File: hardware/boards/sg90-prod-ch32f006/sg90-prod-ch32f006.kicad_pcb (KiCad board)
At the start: 4 copper layers, 12.5 x 10 mm, 21 parts, among them J1 Servo Input, J2 Debug, J3 Motor, J4 Potentiometer, Q1 BRCS150P02ZJ, U1 CH32V006F8U6, U2 DRV8837C, U3 74LVC1G07

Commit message: re-organize shared folders
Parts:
- removed C7: 10µF, Capacitor_SMD:C_0603_1608Metric
- removed R9: 1kΩ, Resistor_SMD:R_0402_1005Metric
- added D1: PESD5V0L1UL, Diode_SMD:D_SOD-882, F.Cu at (109.6, 84.4)
- added NT1: NetTie_2, shared:NetTie-2_SMD_0.2mm, F.Cu at (121.3, 75.5)
- added NT2: NetTie_2, shared:NetTie-2_SMD_0.2mm, F.Cu at (121.3, 77.0)
- added NT3: NetTie_2, shared:NetTie-2_SMD_0.2mm, F.Cu at (121.3, 78.5)
- added NT4: NetTie_2, shared:NetTie-2_SMD_0.2mm, F.Cu at (121.3, 80.0)
- added R7: 10kΩ, Resistor_SMD:R_0402_1005Metric, F.Cu at (0.95, 0.49)
- C1: value 0.1µF -> 10µF; footprint Capacitor_SMD:C_0402_1005Metric -> Capacitor_SMD:C_0603_1608Metric
- C2: value 47nF -> 0.1µF
- C6: value 10µF -> 47nF; footprint Capacitor_SMD:C_0603_1608Metric -> Capacitor_SMD:C_0402_1005Metric
- J1: footprint common:Servo_Output_Pads -> shared:Servo_Output_Pads; moved to B.Cu
- J2: footprint common:Debug_Pads_1x4_P1.27mm -> shared:Debug_Pads_1x4_P1.27mm
- J3: footprint common:Motor_Wire_Pads -> shared:Motor_Wire_Pads; moved to B.Cu
- J4: footprint common:Pot_Wire_Pads -> shared:Pot_Wire_Pads; moved to B.Cu
- Q1: footprint common:DFN-6L_L2.0-W2.0-P0.65-BL_BRCS300PXX -> shared:DFN-6L_L2.0-W2.0-P0.65-BL_BRCS300PXX
- R2: value 0.1Ω 1% -> 1kΩ; footprint Resistor_SMD:R_0603_1608Metric -> Resistor_SMD:R_0402_1005Metric
- R4: value 10kΩ -> 0.1Ω 1%; footprint Resistor_SMD:R_0402_1005Metric -> Resistor_SMD:R_0603_1608Metric
- U1: value CH32V006F8U6 -> 74LVC1G07; footprint common:UQFN-20_L3.0-W3.0-P0.40-BL-EP1.7 -> shared:TDFN-6_L1.0-W1.0-P0.35-BL
- U3: value 74LVC1G07 -> CH32V006F8U6; footprint common:TDFN-6_L1.0-W1.0-P0.35-BL -> shared:UQFN-20_L3.0-W3.0-P0.40-BL-EP1.7
- moved R2 25.9 mm to (125.5, 83.6)
- moved C2 20.3 mm to (125.4, 104.0), turned to -90 degrees
- moved C5 18.4 mm to (119.2, 104.8)
- moved R5 18.1 mm to (125.2, 101.5)
- moved R3 16.6 mm to (119.7, 99.9)
- moved C6 15.8 mm to (122.0, 87.6)
- moved C1 15.1 mm to (107.5, 84.5), turned to -90 degrees
- moved U1 14.4 mm to (121.8, 103.2)
- moved U3 14.2 mm to (117.8, 83.2)
- moved R1 13.9 mm to (118.7, 102.8)
- moved Q1 9.31 mm to (117.9, 90.5)
- moved J2 7.46 mm to (107.9, 106.0)
- moved R4 4.71 mm to (102.0, 96.8)
- moved C3 4.57 mm to (101.0, 93.0), turned to 180 degrees
- moved C4 2.17 mm to (102.9, 93.0), turned to 0 degrees
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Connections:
- C2 pad 1: /SEN_POT -> +5V
- C6 pad 1: +5V -> /SEN_POT
- J3 pad 1: /MOT_B -> /MOT_A
- J3 pad 2: /MOT_A -> /MOT_B
- J4 pad 3: /V_MCU -> +5V
- R1 pad 1: /nRST -> Net-(Q1-G)
- R2 pad 1: /GND_MOT -> +5V
- R2 pad 2: GND -> /DATA
- R4 pad 1: Net-(Q1-G) -> GND
- R4 pad 2: GND -> /GND_MOT
- U1 pad 1: /nRST -> unconnected-(U1-NC-Pad1)
- U1 pad 2: /GND_MOT -> /UART_TX
- U1 pad 3: /GND_MOT -> GND
- U1 pad 4: GND -> /DATA
- U3 pad 1: unconnected-(U3-NC-Pad1) -> /nRST
- U3 pad 2: /UART_TX -> /SEN_I
- U3 pad 3: GND -> /SEN_I
- U3 pad 4: /DATA -> GND

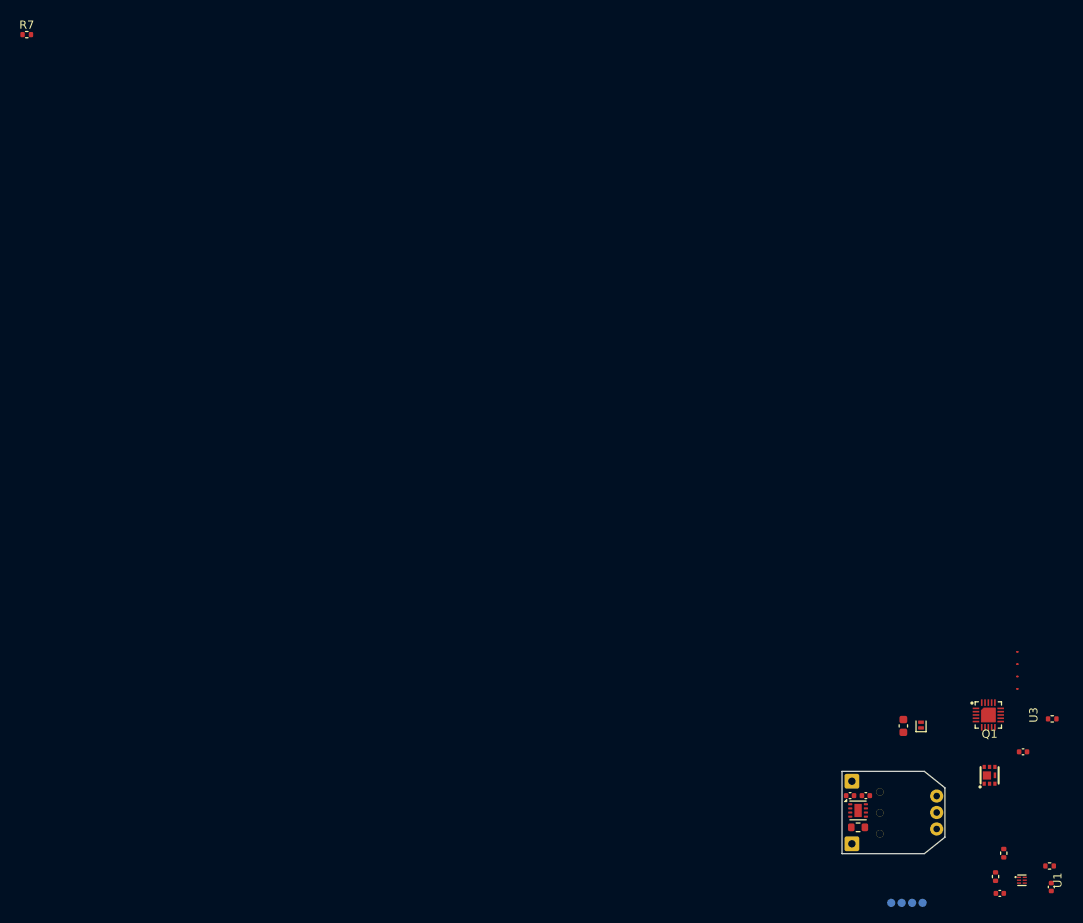
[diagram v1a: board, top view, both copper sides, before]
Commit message: completed initial pass n sg90-prod-ch32f006
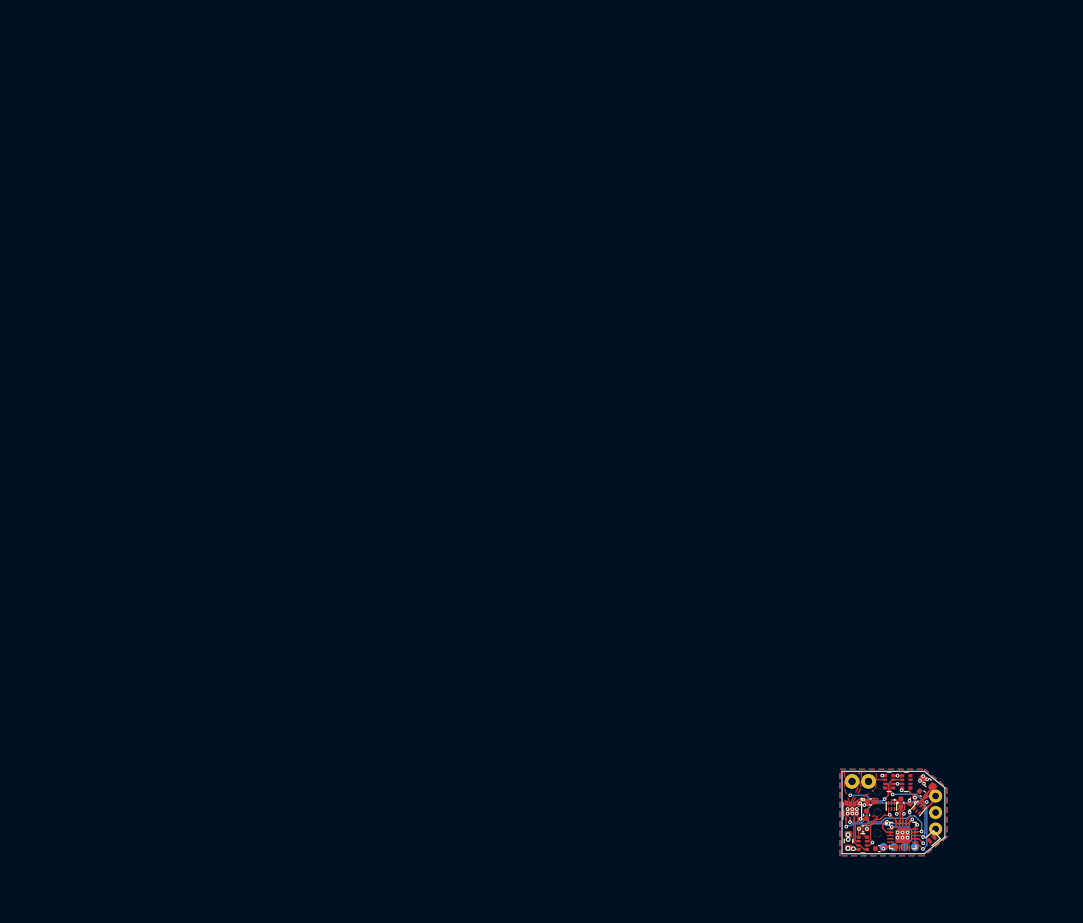
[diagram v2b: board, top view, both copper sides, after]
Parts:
- removed NT3, NT4: NetTie_2, shared:NetTie-2_SMD_0.2mm
- removed Q1: BRCS150P02ZJ, shared:DFN-6L_L2.0-W2.0-P0.65-BL_BRCS300PXX
- removed R2, R5: 1kΩ, Resistor_SMD:R_0402_1005Metric
- removed R3, R7: 10kΩ, Resistor_SMD:R_0402_1005Metric
- removed R4: 0.1Ω 1%, Resistor_SMD:R_0603_1608Metric
- added C2: 1uF, Capacitor_SMD:C_0402_1005Metric, F.Cu at (109.8, 92.7)
- added C3: 1uF, Capacitor_SMD:C_0402_1005Metric, F.Cu at (108.6, 93.6)
- added RN1: 20kΩ, Resistor_SMD:R_Array_Convex_4x0402, F.Cu at (105.7, 91.3)
- added RN2: 10kΩ, Resistor_SMD:R_Array_Convex_4x0402, F.Cu at (107.8, 91.3)
- added RN3: 1kΩ, Resistor_SMD:R_Array_Convex_4x0402, F.Cu at (102.5, 98.7)
- added U1: LDK220PU33R, shared:DFN-6_L1.3-W1.2-P0.40-BL, F.Cu at (109.3, 94.5)
- J2: renamed from J3; moved to F.Cu
- R1: value 10kΩ -> 0.1Ω 1%; footprint Resistor_SMD:R_0402_1005Metric -> Resistor_SMD:R_0603_1608Metric
- U3: renamed from U2; value DRV8837C -> DRV8837DSGR-JSM
- moved NT2 25.6 mm to (105.0, 96.7), turned to 90 degrees
- moved NT1 25.2 mm to (106.4, 95.8), turned to 135 degrees
- moved C5 21.6 mm to (102.5, 97.0), turned to 0 degrees
- moved C4 20.9 mm to (107.2, 93.8), turned to 90 degrees
- moved R1 18.4 mm to (100.8, 98.5)
- moved U2 18.2 mm to (106.0, 94.2), turned to 180 degrees
- moved U4 18.0 mm to (107.4, 97.8)
- moved C8 15.6 mm to (104.5, 99.4), turned to 180 degrees
- moved D1 13.9 mm to (110.9, 98.2), turned to -140.5 degrees
- moved C1 7.51 mm to (110.4, 91.4), turned to 140.5 degrees
- moved J3 6.84 mm to (107.0, 99.2), turned to 0 degrees
- moved J2 3.92 mm to (102.2, 91.2), turned to 180 degrees
- moved C6 3.09 mm to (103.0, 95.3), turned to 90 degrees
- moved C7 0.94 mm to (103.5, 93.7)
- moved U3 0.72 mm to (101.2, 94.9), turned to -90 degrees
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- renumbered C2 to C4, C6 to C5, C3 to C6, C4 to C7, C5 to C8, J2 to J3, U1 to U2, U3 to U4
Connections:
- net /MOT_PH renamed /MOT_IN2
- net /MOT_PWM renamed /MOT_IN1
- C1 pad 1: +5V -> /V_BAT
- C4 pad 1: +5V -> +3.3V
- C6 pad 1: +5V -> +3.3V
- C7 pad 1: +5V -> /V_BAT
- C8 pad 1: +5V -> +3.3V
- J1 pad 1: GND -> /V_BAT
- J1 pad 2: /V_IN -> GND
- J3 pad 1: GND -> +3.3V
- J3 pad 2: /V_IN -> GND
- J4 pad 1: GND -> +3.3V
- J4 pad 3: +5V -> GND
- NT1 pad 1: /DATA -> /UART_RX
- NT1 pad 2: /UART_RX -> /DATA
- R1 pad 1: Net-(Q1-G) -> GND
- R1 pad 2: GND -> /GND_MOT
- U2 pad 6: +5V -> +3.3V
- U3 pad 1: +5V -> /V_BAT
- U3 pad 7: /MOT_EN -> /nSLEEP
- U3 pad 8: +5V -> +3.3V
- U4 pad 11: /SEN_POT -> /SEN_A
- U4 pad 16: /SEN_A -> /SEN_POT
- U4 pad 18: unconnected-(U3-PD4/T1/T2/SCK_/OPO0/A7-Pad18) -> /SEN_BAT
- U4 pad 19: unconnected-(U3-PD5/T2/TX/RX_/MISO_/A5-Pad19) -> /UART_TX
- U4 pad 20: unconnected-(U3-PD6/T2/RX/TX_/MOSI_/A6-Pad20) -> /UART_RX
- U4 pad 6: +5V -> +3.3V
- U4 pad 7: /UART_TX -> unconnected-(U4-PC0/T1C1N_/T1/T2/TX_/MOSI_-Pad7)
- U4 pad 8: /UART_RX -> unconnected-(U4-PC1/T1C2N_/T2/RX_/SDA/NSS-Pad8)
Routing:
- net /MOT_IN1: track 0.00 -> 16.4 mm, vias 0 -> 2
- net /SEN_A: track 0.00 -> 15.4 mm, vias 0 -> 2
- net /DATA: track 0.00 -> 13.9 mm, vias 0 -> 1
- net /MOT_IN2: track 0.00 -> 12.8 mm, vias 0 -> 2
- net +3.3V: track 0.00 -> 11.9 mm, vias 0 -> 4
- net /nRST: track 0.00 -> 11.2 mm, vias 0 -> 2
- net /SEN_POT: track 0.00 -> 9.21 mm, vias 0 -> 2
- net /SEN_BAT: track 0.00 -> 8.62 mm, vias 0 -> 2
- net /MOT_EN: track 0.00 -> 8.54 mm, vias 0 -> 2
- net /MOT_B: track 0.00 -> 7.72 mm, vias 0 -> 2
- net /SEN_B: track 0.00 -> 7.18 mm, vias 0 -> 2
- net /V_BAT: track 0.00 -> 6.26 mm, vias 0 -> 4
- net /UART_TX: track 0.00 -> 5.02 mm
- net /nSLEEP: track 0.00 -> 4.80 mm
- net /POT: track 0.00 -> 4.47 mm
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- added copper zone on In2.Cu, net +3.3V
- added copper zone on F.Cu, net /GND_MOT
- added copper zone on In3.Cu, net /GND_MOT
- added copper zone on In4.Cu, net /GND_MOT
- added copper zone on F.Cu, net /MOT_A
- added copper zone on F.Cu, net /MOT_B
- added copper zone on F.Cu, net /V_BAT
- added copper zone on In5.Cu, net /V_BAT
- added copper zone on B.Cu, net GND
- added copper zone on F.Cu, net GND
- added copper zone on In1.Cu, net GND
- added copper zone on In6.Cu, net GND
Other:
- copper layers 4 -> 8

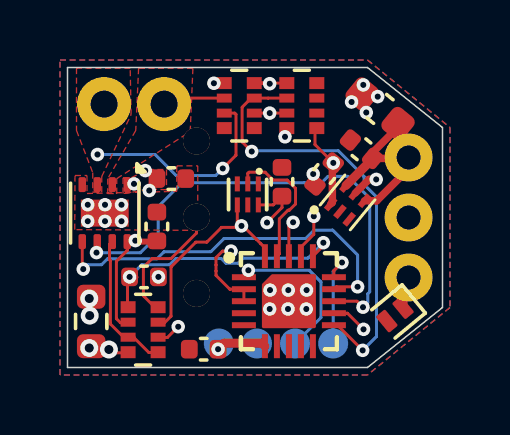
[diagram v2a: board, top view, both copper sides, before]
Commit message: finished first pass design of sg90-prod-ch32f006. It is ready for production
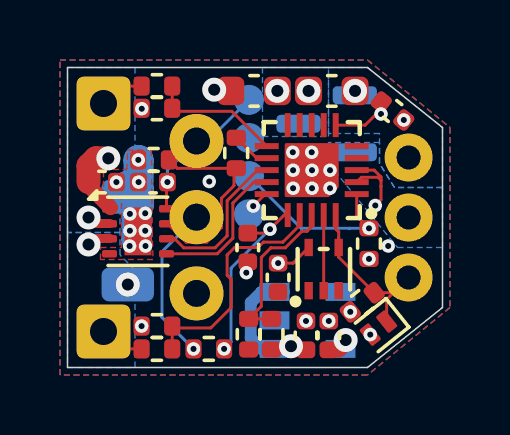
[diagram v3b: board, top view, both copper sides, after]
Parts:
- removed RN1: 20kΩ, Resistor_SMD:R_Array_Convex_4x0402
- removed RN2: 10kΩ, Resistor_SMD:R_Array_Convex_4x0402
- removed RN3: 1kΩ, Resistor_SMD:R_Array_Convex_4x0402
- added C9: 10µF, Capacitor_SMD:C_0603_1608Metric, F.Cu at (106.2, 90.8)
- added Q1: AO3401A, Package_TO_SOT_SMD:SOT-23, B.Cu at (108.6, 91.9)
- added R10: 10kΩ, Resistor_SMD:R_0402_1005Metric, F.Cu at (103.0, 91.4)
- added R11: 20kΩ, Resistor_SMD:R_0402_1005Metric, F.Cu at (103.0, 99.4)
- added R12: 10kΩ, Resistor_SMD:R_0402_1005Metric, F.Cu at (103.0, 98.6)
- added R2: 4.7kΩ, Resistor_SMD:R_0402_1005Metric, F.Cu at (104.7, 99.4)
- added R3: 10kΩ, Resistor_SMD:R_0402_1005Metric, F.Cu at (102.9, 93.1)
- added R4: 0.1Ω 1%, Resistor_SMD:R_1206_3216Metric, B.Cu at (102.0, 95.8)
- added R5: 330Ω, Resistor_SMD:R_0402_1005Metric, F.Cu at (105.6, 92.8)
- added R6: 10kΩ, Resistor_SMD:R_0402_1005Metric, F.Cu at (110.0, 95.9)
- added R7: 20kΩ, Resistor_SMD:R_0402_1005Metric, F.Cu at (106.8, 98.9)
- added R8: 10kΩ, Resistor_SMD:R_0402_1005Metric, F.Cu at (106.0, 98.9)
- added R9: 20kΩ, Resistor_SMD:R_0402_1005Metric, F.Cu at (103.0, 90.6)
- C2, C3: value 1uF -> 1µF
- C5: value 47nF -> 0.1µF
- R1: value 0.1Ω 1% -> 1kΩ; footprint Resistor_SMD:R_0603_1608Metric -> Resistor_SMD:R_0402_1005Metric
- U1: value LDK220PU33R -> TPAP2210K-3.3TRG1; footprint shared:DFN-6_L1.3-W1.2-P0.40-BL -> shared:SOT-23-5_L2.9-W1.6-P0.95-LS2.8-BR; moved to B.Cu
- U2: value 74LVC1G07 -> SN74LVC1G07DRLR_C19829624; footprint shared:TDFN-6_L1.0-W1.0-P0.35-BL -> shared:SOT-553-5_L1.6-W1.2-P0.50-LS1.6-BL
- moved C8 10.1 mm to (110.8, 91.4), turned to -38.659 degrees
- moved R1 9.06 mm to (109.8, 97.8), turned to 38.659 degrees
- moved C2 6.48 mm to (108.0, 98.9), turned to 90 degrees
- moved J3 6.28 mm to (106.0, 93.0), turned to -90 degrees
- moved NT2 6.18 mm to (110.5, 93.9), turned to -90 degrees
- moved C3 5.38 mm to (108.7, 98.9), turned to 90 degrees
- moved U4 4.44 mm to (108.1, 93.4), turned to 90 degrees
- moved U1 4.15 mm to (108.0, 98.4), turned to 180 degrees
- moved J2 3.92 mm to (101.2, 95.0), turned to -90 degrees
- moved C5 3.60 mm to (106.0, 96.0), turned to -90 degrees
- moved U2 3.55 mm to (108.5, 96.7), turned to 0 degrees
- moved C4 3.19 mm to (107.0, 97.0), turned to -90 degrees
- moved NT1 2.68 mm to (109.0, 95.6), turned to -90 degrees
- moved C7 2.31 mm to (101.2, 93.8)
- moved C1 1.72 mm to (108.8, 90.8), turned to 0 degrees
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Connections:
- net /MOT_A renamed /OUTA
- net /MOT_B renamed /OUTB
- net /MOT_IN1 renamed /IN1
- net /MOT_IN2 renamed /IN2
- net /SEN_I renamed /ISNS
- net /SEN_POT renamed /VPOS
- net /UART_RX renamed /RX
- net /UART_TX renamed /TX
- C1 pad 1: /V_BAT -> /VSYS
- C2 pad 1: /V_BAT -> /VSYS
- C6 pad 2: /GND_MOT -> PGND
- C7 pad 1: /V_BAT -> /VSYS
- C7 pad 2: /GND_MOT -> PGND
- J1 pad 1: /V_BAT -> GND
- J1 pad 2: GND -> VIN
- NT2 pad 2: /GND_MOT -> PGND
- R1 pad 1: GND -> +3.3V
- R1 pad 2: /GND_MOT -> /DATA
- U1 pad 1: +3.3V -> /VSYS
- U1 pad 2: unconnected-(U1-N/C-Pad2) -> GND
- U1 pad 3: unconnected-(U1-ADJ/NC-Pad3) -> /VSYS
- U1 pad 4: /V_BAT -> unconnected-(U1-NC-Pad4)
- U1 pad 5: GND -> +3.3V
- U2 pad 5: unconnected-(U2-NC-Pad5) -> +3.3V
- U3 pad 1: /V_BAT -> /VSYS
- U3 pad 4: /GND_MOT -> PGND
- U3 pad 9: /GND_MOT -> PGND
- U4 pad 11: /SEN_A -> /VSNA
- U4 pad 12: /MOT_EN -> /EN
- U4 pad 17: /SEN_B -> /VSNB
- U4 pad 18: /SEN_BAT -> /VINS
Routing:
- net /SEN_A: track 15.4 -> 0.00 mm, vias 2 -> 0
- net /IN1: track 16.4 -> 5.22 mm, vias 2 -> 0
- net /SEN_BAT: track 8.62 -> 0.00 mm, vias 2 -> 0
- net /MOT_EN: track 8.54 -> 0.00 mm, vias 2 -> 0
- net /DATA: track 13.9 -> 5.44 mm, vias 1 -> 0
- net /VSYS: track 0.00 -> 8.30 mm, vias 0 -> 4
- net /VSNB: track 0.00 -> 8.01 mm
- net /IN2: track 12.8 -> 5.02 mm, vias 2 -> 0
- net /SEN_B: track 7.18 -> 0.00 mm, vias 2 -> 0
- net /V_BAT: track 6.26 -> 0.00 mm, vias 4 -> 0
- net /VINS: track 0.00 -> 5.47 mm
- net /OUTB: track 7.72 -> 2.32 mm, vias 2 -> 1
- net /nRST: track 11.2 -> 6.03 mm, vias 2 -> 1
- net /VSNA: track 0.00 -> 4.42 mm
- net PGND: track 0.00 -> 3.48 mm, vias 0 -> 10
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- added copper zone on B.Cu, net /OUTA
- added copper zone on B.Cu, net /OUTB
- added copper zone on B.Cu, net /VSYS
- added copper zone on In4.Cu, net /VSYS
- added copper zone on F.Cu, net PGND
- added copper zone on In3.Cu, net PGND
- added copper zone on B.Cu, net VIN
- removed copper zone on F.Cu, net /GND_MOT
- removed copper zone on In3.Cu, net /GND_MOT
- removed copper zone on In4.Cu, net /GND_MOT
- removed copper zone on F.Cu, net /OUTA
- removed copper zone on F.Cu, net /OUTB
- removed copper zone on F.Cu, net /V_BAT
- removed copper zone on In5.Cu, net /V_BAT
- removed copper zone on In6.Cu, net GND
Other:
- copper layers 8 -> 6
- board text added: "+"
- board text added: "-"
- board text added: "R"
- board text added: "S"

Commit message: redid the PCB after finding a bunch of issues
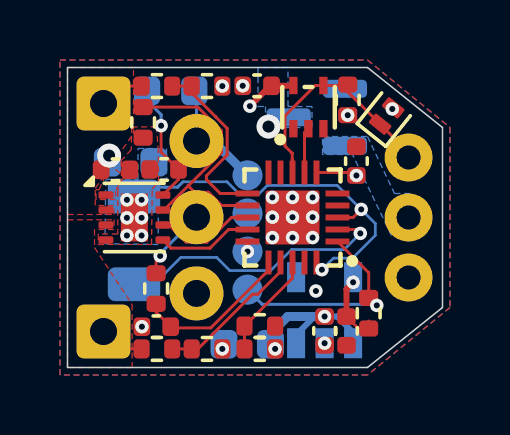
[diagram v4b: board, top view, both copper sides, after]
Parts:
- removed R5: 330Ω, Resistor_SMD:R_0402_1005Metric
- added FB1: 600Ω@100MHz, Inductor_SMD:L_0603_1608Metric, B.Cu at (103.4, 90.8)
- added NT3: NetTie_2, shared:NetTie-2_SMD_0.2mm, B.Cu at (103.2, 96.9)
- C1, NT2: moved to B.Cu
- C8: value 0.1µF -> 10µF; footprint Capacitor_SMD:C_0402_1005Metric -> Capacitor_SMD:C_0603_1608Metric; moved to B.Cu
- C9: value 10µF -> 0.1µF; footprint Capacitor_SMD:C_0603_1608Metric -> Capacitor_SMD:C_0402_1005Metric
- moved C1 8.90 mm to (106.0, 99.2), turned to 180 degrees
- moved C8 8.90 mm to (102.1, 93.2), turned to 0 degrees
- moved NT2 7.28 mm to (103.2, 94.0), turned to 180 degrees
- moved D1 7.07 mm to (110.6, 91.6), turned to 51.341 degrees
- moved R1 6.76 mm to (109.3, 91.1), turned to 90 degrees
- moved C4 6.43 mm to (106.3, 90.6), turned to 180 degrees
- moved U2 5.42 mm to (108.0, 91.3)
- moved C9 4.14 mm to (109.6, 93.1), turned to 90 degrees
- moved C5 4.03 mm to (103.0, 98.6), turned to 180 degrees
- moved NT1 3.04 mm to (107.5, 93.0), turned to 90 degrees
- moved R2 2.67 mm to (103.0, 97.4), turned to -90 degrees
- moved J3 2.52 mm to (106.0, 95.5)
- moved R6 2.32 mm to (110.0, 98.2)
- moved R12 1.83 mm to (104.7, 99.4), turned to 0 degrees
- moved R10 1.83 mm to (104.7, 90.6), turned to 0 degrees
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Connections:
- C6 pad 1: +3.3V -> /3V3_DRV
- C8 pad 1: +3.3V -> /VSYS
- C8 pad 2: GND -> PGND
- C9 pad 1: /VSYS -> +3.3V
- J3 pad 3: /nRST -> /SWDIO
- J3 pad 4: /SWDIO -> /nRST
- NT2 pad 1: /ISNS -> /ISNS+
- R3 pad 1: /nSLEEP -> /EN
- R4 pad 1: PGND -> GND
- R4 pad 2: GND -> PGND
- U3 pad 7: /nSLEEP -> /EN
- U3 pad 8: +3.3V -> /3V3_DRV
- U4 pad 19: /TX -> unconnected-(U4-PD5/T2/TX/RX_/MISO_/A5-Pad19)
- U4 pad 2: /ISNS -> /ISNS-
- U4 pad 20: /RX -> /ISNS+
- U4 pad 3: /ISNS -> /ISNS+
- U4 pad 7: unconnected-(U4-PC0/T1C1N_/T1/T2/TX_/MOSI_-Pad7) -> /TX
- U4 pad 8: unconnected-(U4-PC1/T1C2N_/T2/RX_/SDA/NSS-Pad8) -> /RX
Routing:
- net /ISNS+: track 0.00 -> 11.4 mm, vias 0 -> 2
- net /ISNS-: track 0.00 -> 8.30 mm, vias 0 -> 1
- net /EN: track 1.30 -> 8.66 mm
- net /nSLEEP: track 6.91 -> 0.00 mm
- net /3V3_DRV: track 0.00 -> 4.13 mm, vias 0 -> 1
- net PGND: track 3.48 -> 0.00 mm, vias 10 -> 6
- net /VSNB: track 8.01 -> 4.98 mm
- net /POT: track 5.30 -> 2.42 mm
- net /VSYS: track 8.30 -> 5.45 mm
- net /ISNS: track 1.93 -> 0.00 mm
- net /IN1: track 5.22 -> 3.40 mm
- net /IN2: track 5.02 -> 3.19 mm
- net /DATA: track 5.44 -> 7.19 mm
- net /VSNA: track 4.42 -> 6.11 mm
- net /VINS: track 5.47 -> 3.84 mm
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- added copper zone on F.Cu, net /OUTA
- added copper zone on F.Cu, net /OUTB
- added copper zone on F.Cu, net /VSYS
- added copper zone on B.Cu, net PGND
- removed copper zone on B.Cu, net /OUTA
- removed copper zone on B.Cu, net /OUTB
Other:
- board text removed: "+"
- board text removed: "-"
- board text removed: "R"
- board text removed: "S"
